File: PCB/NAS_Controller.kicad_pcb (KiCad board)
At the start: 4 copper layers, 119.5 x 99.6 mm, 350 parts, among them J1 Barrel_Jack, J10 Conn_01x10, J11 10103594-0001LF, J13 Conn_01x03, J14 20021121-00020C4LF, J15 Conn_01x03, J18 M20-9990246, J2 Conn_01x04, J3 105133-0011, J4 10103594-0001LF, J5 NPPN101BFCN-RC, J6 NPPN101BFCN-RC, J7 Conn_01x03, J8 PPTC081LFBN-RC, J9 PPTC081LFBN-RC, Q1 DMN6068LK3-13, Q10 AOD409, Q11 DMG1026UV-7, Q12 DMG1026UV-7, Q13 DMN6068LK3-13, Q14 DMG1026UV-7, Q2 DMN6068LK3-13, Q3 MMBT3904-TP, Q8 AOD409, Q9 AOD409, SW1 SW_SP3T_1COM_234, U1 ZXCT1110, U10 TS5A3357DCUR, U11 PCA6416APW,118, U12 ZXGD3009E6TA, U13 TS462CDT, U14 AP65211AWU-7, U15 RT7258GSP, U16 RT7258GSP, U17 LM3481MM, U2 TS462CDT, U3 AZ1084CD-3.3, U4 TS462CDT, U5 TS462CDT, U6 TMS320F28035PAGS, U7 MB85RS16, U8 CY7C65634-48AXCT, U9 TS5A3357DCUR, Y1 12MHz

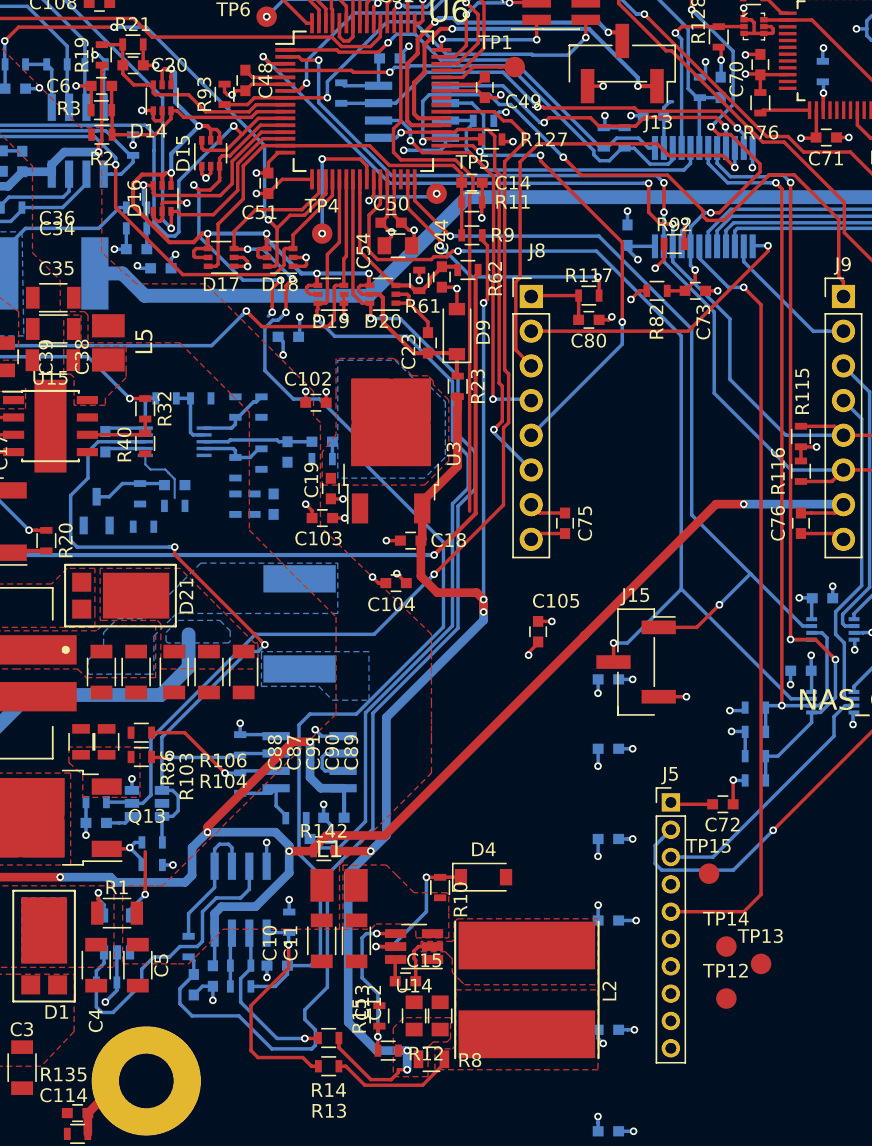
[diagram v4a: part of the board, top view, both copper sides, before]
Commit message: Layout... finished routing, now need to stitch vias, reveiew pours and then silkscreen.
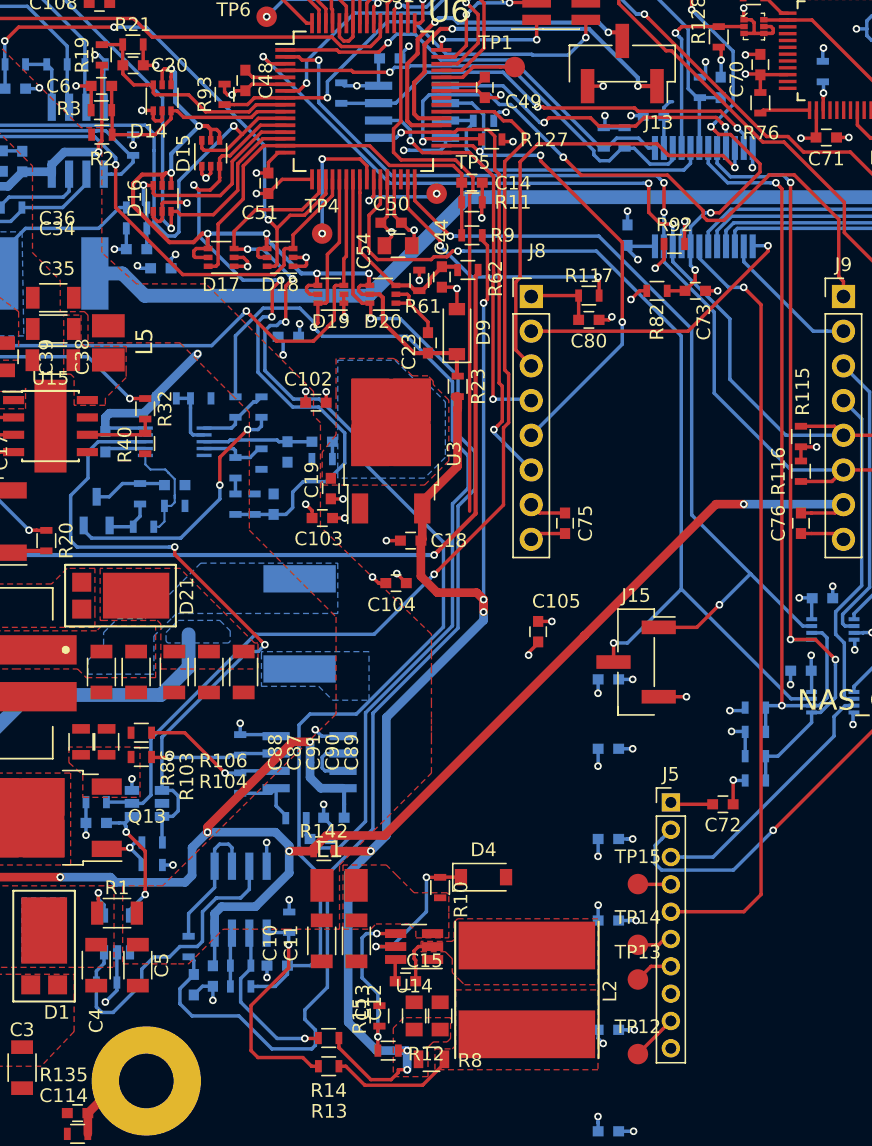
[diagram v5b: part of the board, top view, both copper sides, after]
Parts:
- moved TP13 9.09 mm to (82.4, 86.2)
- moved TP12 7.65 mm to (82.4, 91.7)
- moved TP14 6.48 mm to (82.4, 83.7)
- moved TP15 5.26 mm to (82.4, 79.2)
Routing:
- net ADC_SEPIC_V: track 24.0 -> 49.1 mm
- net Net-(Q3-Pad2): track 0.00 -> 19.4 mm, vias 0 -> 2
- net ADC_SEPIC_I: track 65.6 -> 78.2 mm
- net Vin: track 28.9 -> 38.7 mm, vias 15 -> 17
- net Net-(Q3-Pad1): track 0.00 -> 3.64 mm
- net Net-(R112-Pad1): track 4.86 -> 8.30 mm
- net Net-(J5-Pad9): track 0.00 -> 3.42 mm
- net Net-(J5-Pad7): track 0.00 -> 2.81 mm
- net Net-(J5-Pad6): track 0.00 -> 2.59 mm
- net Net-(J5-Pad4): track 0.00 -> 2.42 mm
- net V_SEPIC: track 36.1 -> 37.3 mm
- net ADC_BATT_I: track 55.5 -> 56.4 mm
- net +3V3: track 108.8 -> 108.4 mm, vias 43 -> 44

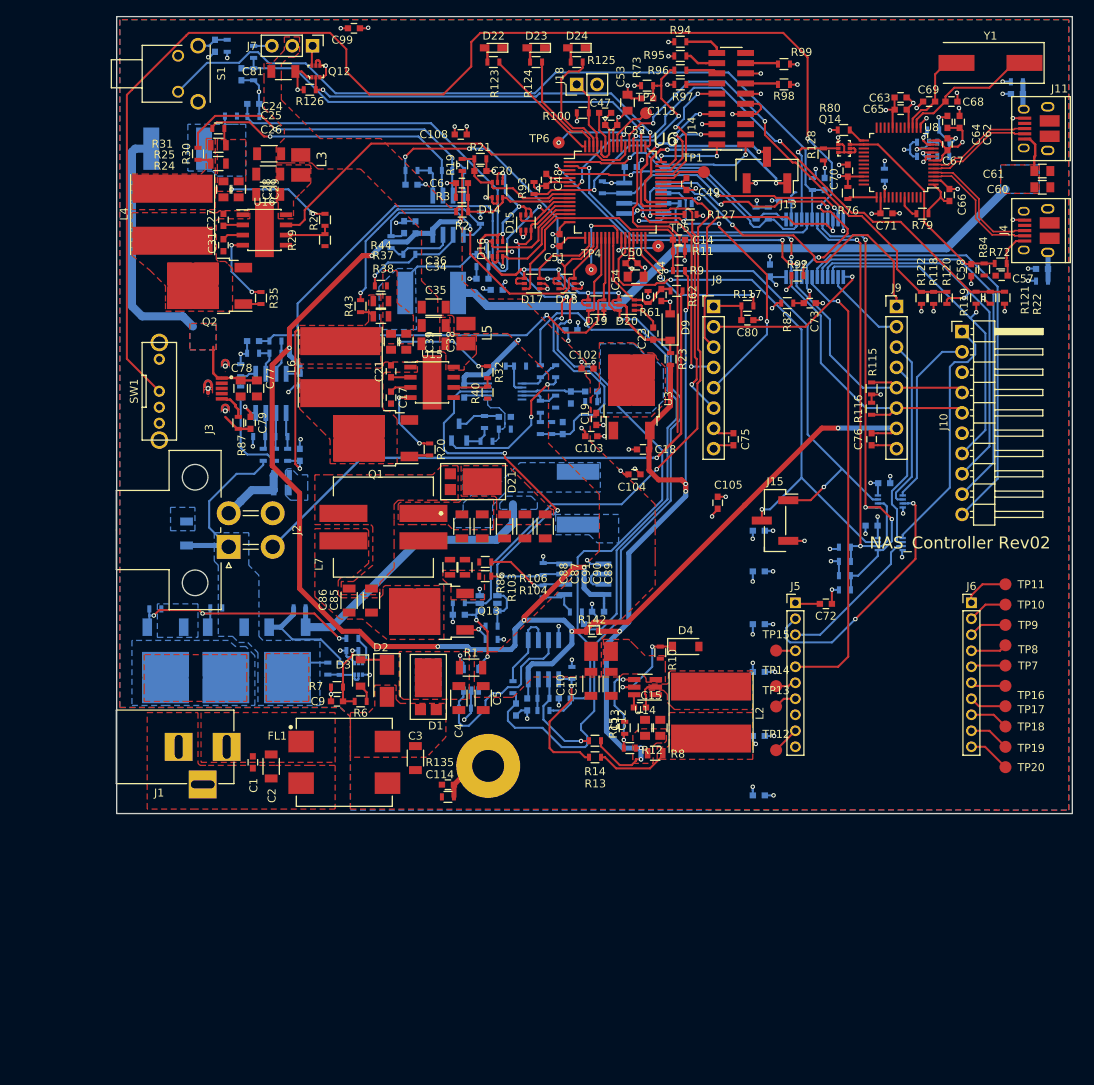
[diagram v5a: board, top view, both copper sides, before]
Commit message: Added stitching vias; one unconnected net left, then silkscreen.
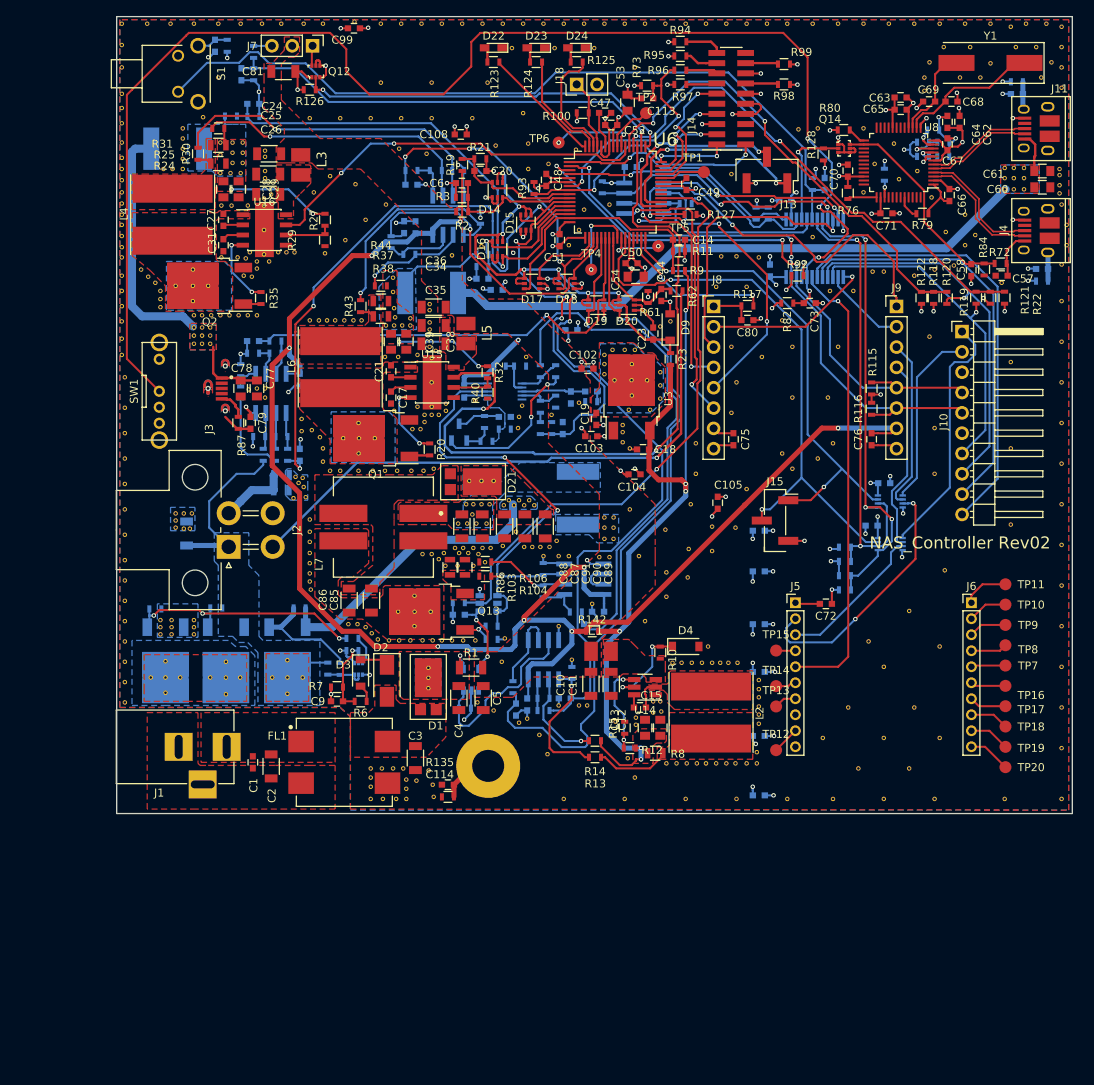
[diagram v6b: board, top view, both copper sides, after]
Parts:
- added REF**: VIA_12_22, CustomFootprints:VIA_12_22, F.Cu at (113.4, 20.2)
- added REF**: VIA_12_22, CustomFootprints:VIA_12_22, F.Cu at (9.65, 75.4)
- added REF**: VIA_12_22, CustomFootprints:VIA_12_22, F.Cu at (111.8, 43.2)
- added REF**: VIA_12_22, CustomFootprints:VIA_12_22, F.Cu at (111.8, 54.0)
- added REF**: VIA_12_22, CustomFootprints:VIA_12_22, F.Cu at (111.8, 63.5)
- added REF**: VIA_12_22, CustomFootprints:VIA_12_22, F.Cu at (103.5, 69.2)
- added REF**: VIA_12_22, CustomFootprints:VIA_12_22, F.Cu at (99.1, 74.3)
- added REF**: VIA_12_22, CustomFootprints:VIA_12_22, F.Cu at (94.0, 78.1)
- added REF**: VIA_12_22, CustomFootprints:VIA_12_22, F.Cu at (102.9, 78.7)
- added REF**: VIA_12_22, CustomFootprints:VIA_12_22, F.Cu at (95.9, 81.3)
- added REF**: VIA_12_22, CustomFootprints:VIA_12_22, F.Cu at (91.4, 86.4)
- added REF**: VIA_12_22, CustomFootprints:VIA_12_22, F.Cu at (99.7, 86.4)
- added REF**: VIA_12_22, CustomFootprints:VIA_12_22, F.Cu at (9.65, 76.3)
- added REF**: VIA_12_22, CustomFootprints:VIA_12_22, F.Cu at (102.9, 90.2)
- added REF**: VIA_12_22, CustomFootprints:VIA_12_22, F.Cu at (95.9, 90.2)
- added REF**: VIA_12_22, CustomFootprints:VIA_12_22, F.Cu at (88.3, 90.2)
- added REF**: VIA_12_22, CustomFootprints:VIA_12_22, F.Cu at (99.1, 94.0)
- added REF**: VIA_12_22, CustomFootprints:VIA_12_22, F.Cu at (92.7, 94.0)
- added REF**: VIA_12_22, CustomFootprints:VIA_12_22, F.Cu at (118.7, 28.6)
- added REF**: VIA_12_22, CustomFootprints:VIA_12_22, F.Cu at (118.7, 26.0)
- added REF**: VIA_12_22, CustomFootprints:VIA_12_22, F.Cu at (118.1, 23.5)
- added REF**: VIA_12_22, CustomFootprints:VIA_12_22, F.Cu at (118.1, 6.35)
- added REF**: VIA_12_22, CustomFootprints:VIA_12_22, F.Cu at (118.1, 3.81)
- added REF**: VIA_12_22, CustomFootprints:VIA_12_22, F.Cu at (9.65, 77.2)
- added REF**: VIA_12_22, CustomFootprints:VIA_12_22, F.Cu at (116.2, 0.89)
- added REF**: VIA_12_22, CustomFootprints:VIA_12_22, F.Cu at (113.7, 0.89)
- added REF**: VIA_12_22, CustomFootprints:VIA_12_22, F.Cu at (109.2, 0.89)
- added REF**: VIA_12_22, CustomFootprints:VIA_12_22, F.Cu at (106.0, 0.89)
- added REF**: VIA_12_22, CustomFootprints:VIA_12_22, F.Cu at (102.9, 0.89)
- added REF**: VIA_12_22, CustomFootprints:VIA_12_22, F.Cu at (99.7, 0.89)
- added REF**: VIA_12_22, CustomFootprints:VIA_12_22, F.Cu at (96.5, 0.89)
- added REF**: VIA_12_22, CustomFootprints:VIA_12_22, F.Cu at (93.3, 0.89)
- added REF**: VIA_12_22, CustomFootprints:VIA_12_22, F.Cu at (90.2, 0.89)
- added REF**: VIA_12_22, CustomFootprints:VIA_12_22, F.Cu at (87.0, 0.89)
- added REF**: VIA_12_22, CustomFootprints:VIA_12_22, F.Cu at (5.46, 76.3)
- added REF**: VIA_12_22, CustomFootprints:VIA_12_22, F.Cu at (83.8, 0.89)
- added REF**: VIA_12_22, CustomFootprints:VIA_12_22, F.Cu at (81.3, 0.89)
- added REF**: VIA_12_22, CustomFootprints:VIA_12_22, F.Cu at (78.7, 0.89)
- added REF**: VIA_12_22, CustomFootprints:VIA_12_22, F.Cu at (76.2, 0.89)
- added REF**: VIA_12_22, CustomFootprints:VIA_12_22, F.Cu at (73.7, 0.89)
- added REF**: VIA_12_22, CustomFootprints:VIA_12_22, F.Cu at (71.1, 0.89)
- added REF**: VIA_12_22, CustomFootprints:VIA_12_22, F.Cu at (68.6, 0.89)
- added REF**: VIA_12_22, CustomFootprints:VIA_12_22, F.Cu at (66.0, 0.89)
- added REF**: VIA_12_22, CustomFootprints:VIA_12_22, F.Cu at (63.5, 0.89)
- added REF**: VIA_12_22, CustomFootprints:VIA_12_22, F.Cu at (61.0, 0.89)
- added REF**: VIA_12_22, CustomFootprints:VIA_12_22, F.Cu at (5.46, 75.4)
- added REF**: VIA_12_22, CustomFootprints:VIA_12_22, F.Cu at (58.4, 0.89)
- added REF**: VIA_12_22, CustomFootprints:VIA_12_22, F.Cu at (55.9, 0.89)
- added REF**: VIA_12_22, CustomFootprints:VIA_12_22, F.Cu at (53.3, 0.89)
- added REF**: VIA_12_22, CustomFootprints:VIA_12_22, F.Cu at (50.8, 0.89)
- added REF**: VIA_12_22, CustomFootprints:VIA_12_22, F.Cu at (48.3, 0.89)
- added REF**: VIA_12_22, CustomFootprints:VIA_12_22, F.Cu at (45.7, 0.89)
- added REF**: VIA_12_22, CustomFootprints:VIA_12_22, F.Cu at (43.2, 0.89)
- added REF**: VIA_12_22, CustomFootprints:VIA_12_22, F.Cu at (40.6, 0.89)
- added REF**: VIA_12_22, CustomFootprints:VIA_12_22, F.Cu at (38.1, 0.89)
- added REF**: VIA_12_22, CustomFootprints:VIA_12_22, F.Cu at (35.6, 0.89)
- added REF**: VIA_12_22, CustomFootprints:VIA_12_22, F.Cu at (6.86, 75.4)
- added REF**: VIA_12_22, CustomFootprints:VIA_12_22, F.Cu at (33.0, 0.89)
- added REF**: VIA_12_22, CustomFootprints:VIA_12_22, F.Cu at (29.7, 0.64)
- added REF**: VIA_12_22, CustomFootprints:VIA_12_22, F.Cu at (25.8, 0.89)
- added REF**: VIA_12_22, CustomFootprints:VIA_12_22, F.Cu at (23.4, 0.89)
- added REF**: VIA_12_22, CustomFootprints:VIA_12_22, F.Cu at (20.6, 0.89)
- added REF**: VIA_12_22, CustomFootprints:VIA_12_22, F.Cu at (18.2, 0.89)
- added REF**: VIA_12_22, CustomFootprints:VIA_12_22, F.Cu at (15.5, 0.89)
- added REF**: VIA_12_22, CustomFootprints:VIA_12_22, F.Cu at (12.7, 0.89)
- added REF**: VIA_12_22, CustomFootprints:VIA_12_22, F.Cu at (9.65, 0.89)
- added REF**: VIA_12_22, CustomFootprints:VIA_12_22, F.Cu at (6.73, 0.89)
- added REF**: VIA_12_22, CustomFootprints:VIA_12_22, F.Cu at (6.86, 76.3)
- added REF**: VIA_12_22, CustomFootprints:VIA_12_22, F.Cu at (3.81, 0.89)
- added REF**: VIA_12_22, CustomFootprints:VIA_12_22, F.Cu at (0.64, 0.89)
- added REF**: VIA_12_22, CustomFootprints:VIA_12_22, F.Cu at (0.64, 3.56)
- added REF**: VIA_12_22, CustomFootprints:VIA_12_22, F.Cu at (0.64, 6.35)
- added REF**: VIA_12_22, CustomFootprints:VIA_12_22, F.Cu at (0.64, 9.65)
- added REF**: VIA_12_22, CustomFootprints:VIA_12_22, F.Cu at (0.64, 11.4)
- added REF**: VIA_12_22, CustomFootprints:VIA_12_22, F.Cu at (0.64, 13.3)
- added REF**: VIA_12_22, CustomFootprints:VIA_12_22, F.Cu at (0.64, 32.4)
- added REF**: VIA_12_22, CustomFootprints:VIA_12_22, F.Cu at (0.64, 34.3)
- added REF**: VIA_12_22, CustomFootprints:VIA_12_22, F.Cu at (0.64, 36.2)
- added REF**: VIA_12_22, CustomFootprints:VIA_12_22, F.Cu at (6.86, 77.2)
- added REF**: VIA_12_22, CustomFootprints:VIA_12_22, F.Cu at (0.64, 38.1)
- added REF**: VIA_12_22, CustomFootprints:VIA_12_22, F.Cu at (0.64, 40.3)
- added REF**: VIA_12_22, CustomFootprints:VIA_12_22, F.Cu at (0.64, 42.3)
- added REF**: VIA_12_22, CustomFootprints:VIA_12_22, F.Cu at (1.02, 45.1)
- added REF**: VIA_12_22, CustomFootprints:VIA_12_22, F.Cu at (1.02, 48.9)
- added REF**: VIA_12_22, CustomFootprints:VIA_12_22, F.Cu at (1.02, 52.1)
- added REF**: VIA_12_22, CustomFootprints:VIA_12_22, F.Cu at (1.02, 55.2)
- added REF**: VIA_12_22, CustomFootprints:VIA_12_22, F.Cu at (1.02, 58.4)
- added REF**: VIA_12_22, CustomFootprints:VIA_12_22, F.Cu at (1.02, 61.6)
- added REF**: VIA_12_22, CustomFootprints:VIA_12_22, F.Cu at (1.02, 64.8)
- added REF**: VIA_12_22, CustomFootprints:VIA_12_22, F.Cu at (5.46, 77.2)
- added REF**: VIA_12_22, CustomFootprints:VIA_12_22, F.Cu at (1.02, 67.9)
- added REF**: VIA_12_22, CustomFootprints:VIA_12_22, F.Cu at (1.02, 70.5)
- added REF**: VIA_12_22, CustomFootprints:VIA_12_22, F.Cu at (1.02, 73.0)
- added REF**: VIA_12_22, CustomFootprints:VIA_12_22, F.Cu at (1.02, 75.6)
- added REF**: VIA_12_22, CustomFootprints:VIA_12_22, F.Cu at (1.02, 78.1)
- added REF**: VIA_12_22, CustomFootprints:VIA_12_22, F.Cu at (1.02, 80.6)
- added REF**: VIA_12_22, CustomFootprints:VIA_12_22, F.Cu at (1.02, 83.2)
- added REF**: VIA_12_22, CustomFootprints:VIA_12_22, F.Cu at (1.02, 85.7)
- added REF**: VIA_12_22, CustomFootprints:VIA_12_22, F.Cu at (6.10, 84.5)
- added REF**: VIA_12_22, CustomFootprints:VIA_12_22, F.Cu at (6.10, 80.6)
- added REF**: VIA_12_22, CustomFootprints:VIA_12_22, F.Cu at (45.6, 28.7)
- added REF**: VIA_12_22, CustomFootprints:VIA_12_22, F.Cu at (4.25, 82.6)
- added REF**: VIA_12_22, CustomFootprints:VIA_12_22, F.Cu at (7.94, 82.6)
- added REF**: VIA_12_22, CustomFootprints:VIA_12_22, F.Cu at (6.10, 82.6)
- added REF**: VIA_12_22, CustomFootprints:VIA_12_22, F.Cu at (13.7, 84.7)
- added REF**: VIA_12_22, CustomFootprints:VIA_12_22, F.Cu at (13.7, 80.6)
- added REF**: VIA_12_22, CustomFootprints:VIA_12_22, F.Cu at (11.7, 82.6)
- added REF**: VIA_12_22, CustomFootprints:VIA_12_22, F.Cu at (15.4, 82.6)
- added REF**: VIA_12_22, CustomFootprints:VIA_12_22, F.Cu at (13.7, 82.6)
- added REF**: VIA_12_22, CustomFootprints:VIA_12_22, F.Cu at (21.3, 84.6)
- added REF**: VIA_12_22, CustomFootprints:VIA_12_22, F.Cu at (21.3, 80.5)
- added REF**: VIA_12_22, CustomFootprints:VIA_12_22, F.Cu at (113.4, 18.9)
- added REF**: VIA_12_22, CustomFootprints:VIA_12_22, F.Cu at (62.1, 63.9)
- added REF**: VIA_12_22, CustomFootprints:VIA_12_22, F.Cu at (19.4, 82.6)
- added REF**: VIA_12_22, CustomFootprints:VIA_12_22, F.Cu at (23.2, 82.6)
- added REF**: VIA_12_22, CustomFootprints:VIA_12_22, F.Cu at (21.3, 82.6)
- added REF**: VIA_12_22, CustomFootprints:VIA_12_22, F.Cu at (41.1, 68.6)
- added REF**: VIA_12_22, CustomFootprints:VIA_12_22, F.Cu at (46.0, 68.2)
- added REF**: VIA_12_22, CustomFootprints:VIA_12_22, F.Cu at (44.6, 68.6)
- added REF**: VIA_12_22, CustomFootprints:VIA_12_22, F.Cu at (42.6, 68.6)
- added REF**: VIA_12_22, CustomFootprints:VIA_12_22, F.Cu at (39.0, 83.9)
- added REF**: VIA_12_22, CustomFootprints:VIA_12_22, F.Cu at (39.0, 81.4)
- added REF**: VIA_12_22, CustomFootprints:VIA_12_22, F.Cu at (39.0, 82.6)
- added REF**: VIA_12_22, CustomFootprints:VIA_12_22, F.Cu at (62.1, 65.3)
- added REF**: VIA_12_22, CustomFootprints:VIA_12_22, F.Cu at (37.2, 76.2)
- added REF**: VIA_12_22, CustomFootprints:VIA_12_22, F.Cu at (37.2, 72.4)
- added REF**: VIA_12_22, CustomFootprints:VIA_12_22, F.Cu at (35.2, 74.4)
- added REF**: VIA_12_22, CustomFootprints:VIA_12_22, F.Cu at (39.2, 74.4)
- added REF**: VIA_12_22, CustomFootprints:VIA_12_22, F.Cu at (34.5, 32.6)
- added REF**: VIA_12_22, CustomFootprints:VIA_12_22, F.Cu at (34.5, 34.4)
- added REF**: VIA_12_22, CustomFootprints:VIA_12_22, F.Cu at (34.7, 36.4)
- added REF**: VIA_12_22, CustomFootprints:VIA_12_22, F.Cu at (34.8, 37.6)
- added REF**: VIA_12_22, CustomFootprints:VIA_12_22, F.Cu at (36.7, 37.7)
- added REF**: VIA_12_22, CustomFootprints:VIA_12_22, F.Cu at (36.7, 38.6)
- added REF**: VIA_12_22, CustomFootprints:VIA_12_22, F.Cu at (61.0, 65.3)
- added REF**: VIA_12_22, CustomFootprints:VIA_12_22, F.Cu at (35.7, 38.6)
- added REF**: VIA_12_22, CustomFootprints:VIA_12_22, F.Cu at (34.7, 38.6)
- added REF**: VIA_12_22, CustomFootprints:VIA_12_22, F.Cu at (33.7, 38.6)
- added REF**: VIA_12_22, CustomFootprints:VIA_12_22, F.Cu at (52.2, 61.1)
- added REF**: VIA_12_22, CustomFootprints:VIA_12_22, F.Cu at (51.6, 60.5)
- added REF**: VIA_12_22, CustomFootprints:VIA_12_22, F.Cu at (50.9, 61.1)
- added REF**: VIA_12_22, CustomFootprints:VIA_12_22, F.Cu at (50.3, 60.5)
- added REF**: VIA_12_22, CustomFootprints:VIA_12_22, F.Cu at (49.7, 61.1)
- added REF**: VIA_12_22, CustomFootprints:VIA_12_22, F.Cu at (49.0, 60.5)
- added REF**: VIA_12_22, CustomFootprints:VIA_12_22, F.Cu at (48.4, 61.1)
- added REF**: VIA_12_22, CustomFootprints:VIA_12_22, F.Cu at (61.0, 63.9)
- added REF**: VIA_12_22, CustomFootprints:VIA_12_22, F.Cu at (44.1, 58.0)
- added REF**: VIA_12_22, CustomFootprints:VIA_12_22, F.Cu at (47.1, 58.0)
- added REF**: VIA_12_22, CustomFootprints:VIA_12_22, F.Cu at (45.6, 58.0)
- added REF**: VIA_12_22, CustomFootprints:VIA_12_22, F.Cu at (44.5, 62.2)
- added REF**: VIA_12_22, CustomFootprints:VIA_12_22, F.Cu at (43.7, 61.0)
- added REF**: VIA_12_22, CustomFootprints:VIA_12_22, F.Cu at (44.6, 61.0)
- added REF**: VIA_12_22, CustomFootprints:VIA_12_22, F.Cu at (45.6, 61.0)
- added REF**: VIA_12_22, CustomFootprints:VIA_12_22, F.Cu at (46.6, 61.0)
- added REF**: VIA_12_22, CustomFootprints:VIA_12_22, F.Cu at (46.2, 63.4)
- added REF**: VIA_12_22, CustomFootprints:VIA_12_22, F.Cu at (45.0, 63.4)
- added REF**: VIA_12_22, CustomFootprints:VIA_12_22, F.Cu at (62.1, 62.6)
- added REF**: VIA_12_22, CustomFootprints:VIA_12_22, F.Cu at (43.8, 63.4)
- added REF**: VIA_12_22, CustomFootprints:VIA_12_22, F.Cu at (42.7, 63.4)
- added REF**: VIA_12_22, CustomFootprints:VIA_12_22, F.Cu at (64.4, 47.4)
- added REF**: VIA_12_22, CustomFootprints:VIA_12_22, F.Cu at (64.4, 43.4)
- added REF**: VIA_12_22, CustomFootprints:VIA_12_22, F.Cu at (66.3, 45.5)
- added REF**: VIA_12_22, CustomFootprints:VIA_12_22, F.Cu at (62.2, 45.5)
- added REF**: VIA_12_22, CustomFootprints:VIA_12_22, F.Cu at (64.4, 45.4)
- added REF**: VIA_12_22, CustomFootprints:VIA_12_22, F.Cu at (61.0, 43.4)
- added REF**: VIA_12_22, CustomFootprints:VIA_12_22, F.Cu at (61.0, 44.7)
- added REF**: VIA_12_22, CustomFootprints:VIA_12_22, F.Cu at (61.0, 42.3)
- added REF**: VIA_12_22, CustomFootprints:VIA_12_22, F.Cu at (61.0, 62.6)
- added REF**: VIA_12_22, CustomFootprints:VIA_12_22, F.Cu at (62.0, 41.7)
- added REF**: VIA_12_22, CustomFootprints:VIA_12_22, F.Cu at (63.5, 41.7)
- added REF**: VIA_12_22, CustomFootprints:VIA_12_22, F.Cu at (64.8, 41.7)
- added REF**: VIA_12_22, CustomFootprints:VIA_12_22, F.Cu at (67.9, 44.5)
- added REF**: VIA_12_22, CustomFootprints:VIA_12_22, F.Cu at (67.9, 46.1)
- added REF**: VIA_12_22, CustomFootprints:VIA_12_22, F.Cu at (67.9, 47.8)
- added REF**: VIA_12_22, CustomFootprints:VIA_12_22, F.Cu at (64.0, 49.1)
- added REF**: VIA_12_22, CustomFootprints:VIA_12_22, F.Cu at (66.7, 49.1)
- added REF**: VIA_12_22, CustomFootprints:VIA_12_22, F.Cu at (64.1, 61.6)
- added REF**: VIA_12_22, CustomFootprints:VIA_12_22, F.Cu at (65.3, 67.4)
- added REF**: VIA_12_22, CustomFootprints:VIA_12_22, F.Cu at (41.9, 29.8)
- added REF**: VIA_12_22, CustomFootprints:VIA_12_22, F.Cu at (74.4, 63.8)
- added REF**: VIA_12_22, CustomFootprints:VIA_12_22, F.Cu at (71.5, 66.5)
- added REF**: VIA_12_22, CustomFootprints:VIA_12_22, F.Cu at (68.7, 69.5)
- added REF**: VIA_12_22, CustomFootprints:VIA_12_22, F.Cu at (77.3, 63.9)
- added REF**: VIA_12_22, CustomFootprints:VIA_12_22, F.Cu at (74.4, 66.8)
- added REF**: VIA_12_22, CustomFootprints:VIA_12_22, F.Cu at (71.4, 70.1)
- added REF**: VIA_12_22, CustomFootprints:VIA_12_22, F.Cu at (68.7, 72.5)
- added REF**: VIA_12_22, CustomFootprints:VIA_12_22, F.Cu at (66.0, 75.6)
- added REF**: VIA_12_22, CustomFootprints:VIA_12_22, F.Cu at (48.1, 80.6)
- added REF**: VIA_12_22, CustomFootprints:VIA_12_22, F.Cu at (52.8, 89.8)
- added REF**: VIA_12_22, CustomFootprints:VIA_12_22, F.Cu at (9.53, 35.6)
- added REF**: VIA_12_22, CustomFootprints:VIA_12_22, F.Cu at (53.8, 92.2)
- added REF**: VIA_12_22, CustomFootprints:VIA_12_22, F.Cu at (55.9, 97.8)
- added REF**: VIA_12_22, CustomFootprints:VIA_12_22, F.Cu at (64.8, 95.1)
- added REF**: VIA_12_22, CustomFootprints:VIA_12_22, F.Cu at (63.5, 97.8)
- added REF**: VIA_12_22, CustomFootprints:VIA_12_22, F.Cu at (71.1, 97.8)
- added REF**: VIA_12_22, CustomFootprints:VIA_12_22, F.Cu at (77.5, 97.8)
- added REF**: VIA_12_22, CustomFootprints:VIA_12_22, F.Cu at (83.8, 97.8)
- added REF**: VIA_12_22, CustomFootprints:VIA_12_22, F.Cu at (89.5, 97.8)
- added REF**: VIA_12_22, CustomFootprints:VIA_12_22, F.Cu at (95.9, 97.8)
- added REF**: VIA_12_22, CustomFootprints:VIA_12_22, F.Cu at (102.2, 97.8)
- added REF**: VIA_12_22, CustomFootprints:VIA_12_22, F.Cu at (9.53, 31.6)
- added REF**: VIA_12_22, CustomFootprints:VIA_12_22, F.Cu at (111.0, 97.8)
- added REF**: VIA_12_22, CustomFootprints:VIA_12_22, F.Cu at (118.1, 97.8)
- added REF**: VIA_12_22, CustomFootprints:VIA_12_22, F.Cu at (118.1, 91.4)
- added REF**: VIA_12_22, CustomFootprints:VIA_12_22, F.Cu at (118.1, 86.4)
- added REF**: VIA_12_22, CustomFootprints:VIA_12_22, F.Cu at (118.1, 81.3)
- added REF**: VIA_12_22, CustomFootprints:VIA_12_22, F.Cu at (118.1, 76.2)
- added REF**: VIA_12_22, CustomFootprints:VIA_12_22, F.Cu at (118.1, 71.1)
- added REF**: VIA_12_22, CustomFootprints:VIA_12_22, F.Cu at (118.1, 66.0)
- added REF**: VIA_12_22, CustomFootprints:VIA_12_22, F.Cu at (118.1, 61.0)
- added REF**: VIA_12_22, CustomFootprints:VIA_12_22, F.Cu at (118.1, 55.9)
- added REF**: VIA_12_22, CustomFootprints:VIA_12_22, F.Cu at (7.37, 33.7)
- added REF**: VIA_12_22, CustomFootprints:VIA_12_22, F.Cu at (118.1, 50.8)
- added REF**: VIA_12_22, CustomFootprints:VIA_12_22, F.Cu at (118.1, 45.7)
- added REF**: VIA_12_22, CustomFootprints:VIA_12_22, F.Cu at (118.1, 40.6)
- added REF**: VIA_12_22, CustomFootprints:VIA_12_22, F.Cu at (118.1, 35.6)
- added REF**: VIA_12_22, CustomFootprints:VIA_12_22, F.Cu at (118.1, 31.0)
- added REF**: VIA_12_22, CustomFootprints:VIA_12_22, F.Cu at (118.1, 8.89)
- added REF**: VIA_12_22, CustomFootprints:VIA_12_22, F.Cu at (116.8, 5.72)
- added REF**: VIA_12_22, CustomFootprints:VIA_12_22, F.Cu at (115.6, 7.62)
- added REF**: VIA_12_22, CustomFootprints:VIA_12_22, F.Cu at (105.4, 7.62)
- added REF**: VIA_12_22, CustomFootprints:VIA_12_22, F.Cu at (108.0, 7.62)
- added REF**: VIA_12_22, CustomFootprints:VIA_12_22, F.Cu at (112.1, 18.9)
- added REF**: VIA_12_22, CustomFootprints:VIA_12_22, F.Cu at (11.4, 33.7)
- added REF**: VIA_12_22, CustomFootprints:VIA_12_22, F.Cu at (109.2, 5.84)
- added REF**: VIA_12_22, CustomFootprints:VIA_12_22, F.Cu at (101.0, 9.27)
- added REF**: VIA_12_22, CustomFootprints:VIA_12_22, F.Cu at (101.0, 7.62)
- added REF**: VIA_12_22, CustomFootprints:VIA_12_22, F.Cu at (101.6, 5.72)
- added REF**: VIA_12_22, CustomFootprints:VIA_12_22, F.Cu at (103.4, 3.81)
- added REF**: VIA_12_22, CustomFootprints:VIA_12_22, F.Cu at (106.7, 3.81)
- added REF**: VIA_12_22, CustomFootprints:VIA_12_22, F.Cu at (112.4, 3.81)
- added REF**: VIA_12_22, CustomFootprints:VIA_12_22, F.Cu at (114.9, 3.81)
- added REF**: VIA_12_22, CustomFootprints:VIA_12_22, F.Cu at (111.8, 1.27)
- added REF**: VIA_12_22, CustomFootprints:VIA_12_22, F.Cu at (118.1, 1.27)
- added REF**: VIA_12_22, CustomFootprints:VIA_12_22, F.Cu at (9.53, 33.7)
- added REF**: VIA_12_22, CustomFootprints:VIA_12_22, F.Cu at (83.2, 38.0)
- added REF**: VIA_12_22, CustomFootprints:VIA_12_22, F.Cu at (78.7, 33.8)
- added REF**: VIA_12_22, CustomFootprints:VIA_12_22, F.Cu at (74.9, 33.8)
- added REF**: VIA_12_22, CustomFootprints:VIA_12_22, F.Cu at (75.6, 30.0)
- added REF**: VIA_12_22, CustomFootprints:VIA_12_22, F.Cu at (77.5, 30.0)
- added REF**: VIA_12_22, CustomFootprints:VIA_12_22, F.Cu at (80.3, 30.1)
- added REF**: VIA_12_22, CustomFootprints:VIA_12_22, F.Cu at (87.0, 27.6)
- added REF**: VIA_12_22, CustomFootprints:VIA_12_22, F.Cu at (92.1, 34.3)
- added REF**: VIA_12_22, CustomFootprints:VIA_12_22, F.Cu at (89.2, 34.3)
- added REF**: VIA_12_22, CustomFootprints:VIA_12_22, F.Cu at (94.5, 31.9)
- added REF**: VIA_12_22, CustomFootprints:VIA_12_22, F.Cu at (30.2, 54.6)
- added REF**: VIA_12_22, CustomFootprints:VIA_12_22, F.Cu at (95.9, 31.9)
- added REF**: VIA_12_22, CustomFootprints:VIA_12_22, F.Cu at (99.7, 32.4)
- added REF**: VIA_12_22, CustomFootprints:VIA_12_22, F.Cu at (102.2, 31.6)
- added REF**: VIA_12_22, CustomFootprints:VIA_12_22, F.Cu at (104.6, 31.1)
- added REF**: VIA_12_22, CustomFootprints:VIA_12_22, F.Cu at (110.6, 33.3)
- added REF**: VIA_12_22, CustomFootprints:VIA_12_22, F.Cu at (106.0, 28.6)
- added REF**: VIA_12_22, CustomFootprints:VIA_12_22, F.Cu at (107.3, 27.3)
- added REF**: VIA_12_22, CustomFootprints:VIA_12_22, F.Cu at (106.0, 24.8)
- added REF**: VIA_12_22, CustomFootprints:VIA_12_22, F.Cu at (103.6, 26.9)
- added REF**: VIA_12_22, CustomFootprints:VIA_12_22, F.Cu at (101.9, 22.6)
- added REF**: VIA_12_22, CustomFootprints:VIA_12_22, F.Cu at (30.2, 50.8)
- added REF**: VIA_12_22, CustomFootprints:VIA_12_22, F.Cu at (93.3, 22.0)
- added REF**: VIA_12_22, CustomFootprints:VIA_12_22, F.Cu at (94.7, 18.4)
- added REF**: VIA_12_22, CustomFootprints:VIA_12_22, F.Cu at (97.8, 20.3)
- added REF**: VIA_12_22, CustomFootprints:VIA_12_22, F.Cu at (100.1, 19.3)
- added REF**: VIA_12_22, CustomFootprints:VIA_12_22, F.Cu at (97.2, 15.9)
- added REF**: VIA_12_22, CustomFootprints:VIA_12_22, F.Cu at (93.3, 14.0)
- added REF**: VIA_12_22, CustomFootprints:VIA_12_22, F.Cu at (87.6, 14.0)
- added REF**: VIA_12_22, CustomFootprints:VIA_12_22, F.Cu at (85.2, 14.1)
- added REF**: VIA_12_22, CustomFootprints:VIA_12_22, F.Cu at (64.8, 6.35)
- added REF**: VIA_12_22, CustomFootprints:VIA_12_22, F.Cu at (57.4, 16.6)
- added REF**: VIA_12_22, CustomFootprints:VIA_12_22, F.Cu at (28.3, 52.7)
- added REF**: VIA_12_22, CustomFootprints:VIA_12_22, F.Cu at (54.0, 18.4)
- added REF**: VIA_12_22, CustomFootprints:VIA_12_22, F.Cu at (38.7, 17.1)
- added REF**: VIA_12_22, CustomFootprints:VIA_12_22, F.Cu at (47.4, 16.1)
- added REF**: VIA_12_22, CustomFootprints:VIA_12_22, F.Cu at (44.5, 12.7)
- added REF**: VIA_12_22, CustomFootprints:VIA_12_22, F.Cu at (39.4, 12.7)
- added REF**: VIA_12_22, CustomFootprints:VIA_12_22, F.Cu at (35.6, 12.7)
- added REF**: VIA_12_22, CustomFootprints:VIA_12_22, F.Cu at (31.8, 12.7)
- added REF**: VIA_12_22, CustomFootprints:VIA_12_22, F.Cu at (27.9, 12.7)
- added REF**: VIA_12_22, CustomFootprints:VIA_12_22, F.Cu at (24.1, 12.7)
- added REF**: VIA_12_22, CustomFootprints:VIA_12_22, F.Cu at (35.3, 16.5)
- added REF**: VIA_12_22, CustomFootprints:VIA_12_22, F.Cu at (32.3, 52.7)
- added REF**: VIA_12_22, CustomFootprints:VIA_12_22, F.Cu at (26.7, 19.9)
- added REF**: VIA_12_22, CustomFootprints:VIA_12_22, F.Cu at (24.6, 22.0)
- added REF**: VIA_12_22, CustomFootprints:VIA_12_22, F.Cu at (10.8, 12.6)
- added REF**: VIA_12_22, CustomFootprints:VIA_12_22, F.Cu at (8.26, 14.0)
- added REF**: VIA_12_22, CustomFootprints:VIA_12_22, F.Cu at (8.26, 15.2)
- added REF**: VIA_12_22, CustomFootprints:VIA_12_22, F.Cu at (8.26, 16.5)
- added REF**: VIA_12_22, CustomFootprints:VIA_12_22, F.Cu at (8.26, 17.8)
- added REF**: VIA_12_22, CustomFootprints:VIA_12_22, F.Cu at (5.84, 19.1)
- added REF**: VIA_12_22, CustomFootprints:VIA_12_22, F.Cu at (6.99, 19.1)
- added REF**: VIA_12_22, CustomFootprints:VIA_12_22, F.Cu at (8.26, 19.1)
- added REF**: VIA_12_22, CustomFootprints:VIA_12_22, F.Cu at (30.3, 52.7)
- added REF**: VIA_12_22, CustomFootprints:VIA_12_22, F.Cu at (0.64, 15.7)
- added REF**: VIA_12_22, CustomFootprints:VIA_12_22, F.Cu at (0.64, 17.7)
- added REF**: VIA_12_22, CustomFootprints:VIA_12_22, F.Cu at (0.64, 19.1)
- added REF**: VIA_12_22, CustomFootprints:VIA_12_22, F.Cu at (0.64, 20.4)
- added REF**: VIA_12_22, CustomFootprints:VIA_12_22, F.Cu at (0.64, 22.0)
- added REF**: VIA_12_22, CustomFootprints:VIA_12_22, F.Cu at (0.64, 23.4)
- added REF**: VIA_12_22, CustomFootprints:VIA_12_22, F.Cu at (0.64, 24.8)
- added REF**: VIA_12_22, CustomFootprints:VIA_12_22, F.Cu at (0.64, 26.0)
- added REF**: VIA_12_22, CustomFootprints:VIA_12_22, F.Cu at (0.64, 27.4)
- added REF**: VIA_12_22, CustomFootprints:VIA_12_22, F.Cu at (0.64, 28.8)
- added REF**: VIA_12_22, CustomFootprints:VIA_12_22, F.Cu at (18.5, 47.6)
- added REF**: VIA_12_22, CustomFootprints:VIA_12_22, F.Cu at (0.64, 30.1)
- added REF**: VIA_12_22, CustomFootprints:VIA_12_22, F.Cu at (34.0, 78.0)
- added REF**: VIA_12_22, CustomFootprints:VIA_12_22, F.Cu at (35.3, 78.0)
- added REF**: VIA_12_22, CustomFootprints:VIA_12_22, F.Cu at (36.7, 78.0)
- added REF**: VIA_12_22, CustomFootprints:VIA_12_22, F.Cu at (38.2, 78.0)
- added REF**: VIA_12_22, CustomFootprints:VIA_12_22, F.Cu at (39.5, 78.0)
- added REF**: VIA_12_22, CustomFootprints:VIA_12_22, F.Cu at (40.6, 78.0)
- added REF**: VIA_12_22, CustomFootprints:VIA_12_22, F.Cu at (41.9, 78.0)
- added REF**: VIA_12_22, CustomFootprints:VIA_12_22, F.Cu at (43.3, 78.0)
- added REF**: VIA_12_22, CustomFootprints:VIA_12_22, F.Cu at (44.8, 78.0)
- added REF**: VIA_12_22, CustomFootprints:VIA_12_22, F.Cu at (18.5, 46.5)
- added REF**: VIA_12_22, CustomFootprints:VIA_12_22, F.Cu at (32.6, 77.9)
- added REF**: VIA_12_22, CustomFootprints:VIA_12_22, F.Cu at (31.9, 77.1)
- added REF**: VIA_12_22, CustomFootprints:VIA_12_22, F.Cu at (31.1, 76.3)
- added REF**: VIA_12_22, CustomFootprints:VIA_12_22, F.Cu at (30.1, 75.9)
- added REF**: VIA_12_22, CustomFootprints:VIA_12_22, F.Cu at (29.0, 75.9)
- added REF**: VIA_12_22, CustomFootprints:VIA_12_22, F.Cu at (24.3, 71.6)
- added REF**: VIA_12_22, CustomFootprints:VIA_12_22, F.Cu at (24.1, 70.6)
- added REF**: VIA_12_22, CustomFootprints:VIA_12_22, F.Cu at (24.1, 69.6)
- added REF**: VIA_12_22, CustomFootprints:VIA_12_22, F.Cu at (24.1, 68.3)
- added REF**: VIA_12_22, CustomFootprints:VIA_12_22, F.Cu at (24.1, 67.1)
- added REF**: VIA_12_22, CustomFootprints:VIA_12_22, F.Cu at (17.5, 46.5)
- added REF**: VIA_12_22, CustomFootprints:VIA_12_22, F.Cu at (24.1, 65.7)
- added REF**: VIA_12_22, CustomFootprints:VIA_12_22, F.Cu at (24.1, 64.4)
- added REF**: VIA_12_22, CustomFootprints:VIA_12_22, F.Cu at (24.1, 62.9)
- added REF**: VIA_12_22, CustomFootprints:VIA_12_22, F.Cu at (23.1, 50.3)
- added REF**: VIA_12_22, CustomFootprints:VIA_12_22, F.Cu at (24.4, 51.7)
- added REF**: VIA_12_22, CustomFootprints:VIA_12_22, F.Cu at (23.1, 51.8)
- added REF**: VIA_12_22, CustomFootprints:VIA_12_22, F.Cu at (25.4, 52.6)
- added REF**: VIA_12_22, CustomFootprints:VIA_12_22, F.Cu at (25.8, 54.0)
- added REF**: VIA_12_22, CustomFootprints:VIA_12_22, F.Cu at (25.8, 55.6)
- added REF**: VIA_12_22, CustomFootprints:VIA_12_22, F.Cu at (26.7, 56.8)
- added REF**: VIA_12_22, CustomFootprints:VIA_12_22, F.Cu at (112.1, 20.2)
- added REF**: VIA_12_22, CustomFootprints:VIA_12_22, F.Cu at (16.5, 46.6)
- added REF**: VIA_12_22, CustomFootprints:VIA_12_22, F.Cu at (27.9, 56.8)
- added REF**: VIA_12_22, CustomFootprints:VIA_12_22, F.Cu at (30.2, 56.8)
- added REF**: VIA_12_22, CustomFootprints:VIA_12_22, F.Cu at (32.0, 56.8)
- added REF**: VIA_12_22, CustomFootprints:VIA_12_22, F.Cu at (33.5, 56.8)
- added REF**: VIA_12_22, CustomFootprints:VIA_12_22, F.Cu at (35.1, 56.8)
- added REF**: VIA_12_22, CustomFootprints:VIA_12_22, F.Cu at (36.8, 56.8)
- added REF**: VIA_12_22, CustomFootprints:VIA_12_22, F.Cu at (38.4, 56.8)
- added REF**: VIA_12_22, CustomFootprints:VIA_12_22, F.Cu at (39.6, 56.5)
- added REF**: VIA_12_22, CustomFootprints:VIA_12_22, F.Cu at (24.1, 38.0)
- added REF**: VIA_12_22, CustomFootprints:VIA_12_22, F.Cu at (25.3, 38.0)
- added REF**: VIA_12_22, CustomFootprints:VIA_12_22, F.Cu at (9.65, 39.9)
- added REF**: VIA_12_22, CustomFootprints:VIA_12_22, F.Cu at (26.3, 38.0)
- added REF**: VIA_12_22, CustomFootprints:VIA_12_22, F.Cu at (27.3, 38.0)
- added REF**: VIA_12_22, CustomFootprints:VIA_12_22, F.Cu at (28.4, 38.0)
- added REF**: VIA_12_22, CustomFootprints:VIA_12_22, F.Cu at (29.6, 38.0)
- added REF**: VIA_12_22, CustomFootprints:VIA_12_22, F.Cu at (30.6, 38.0)
- added REF**: VIA_12_22, CustomFootprints:VIA_12_22, F.Cu at (17.5, 37.3)
- added REF**: VIA_12_22, CustomFootprints:VIA_12_22, F.Cu at (16.4, 37.3)
- added REF**: VIA_12_22, CustomFootprints:VIA_12_22, F.Cu at (15.2, 37.3)
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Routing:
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- added copper zone on B.Cu, net Net-(C21-Pad2)
- added copper zone on B.Cu, net Net-(C27-Pad2)

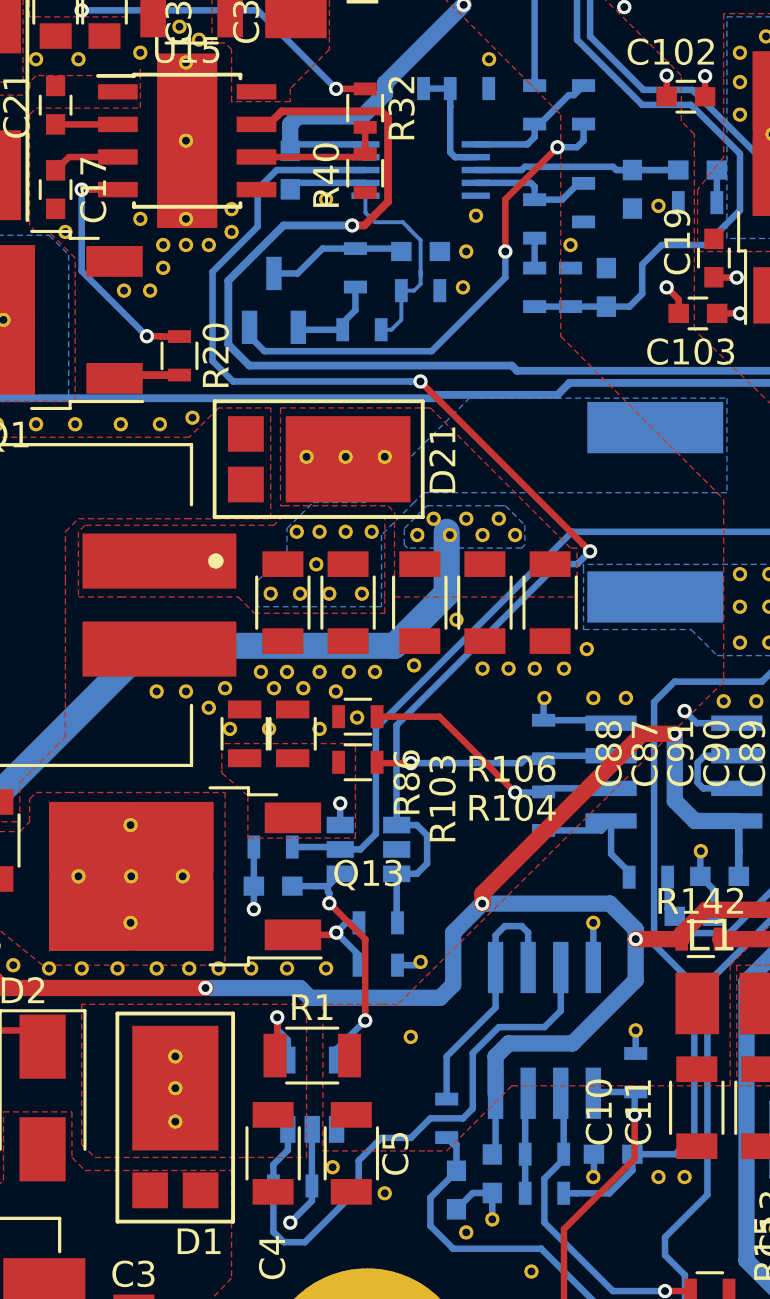
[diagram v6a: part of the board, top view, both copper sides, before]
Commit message: Fixed last missing connection.
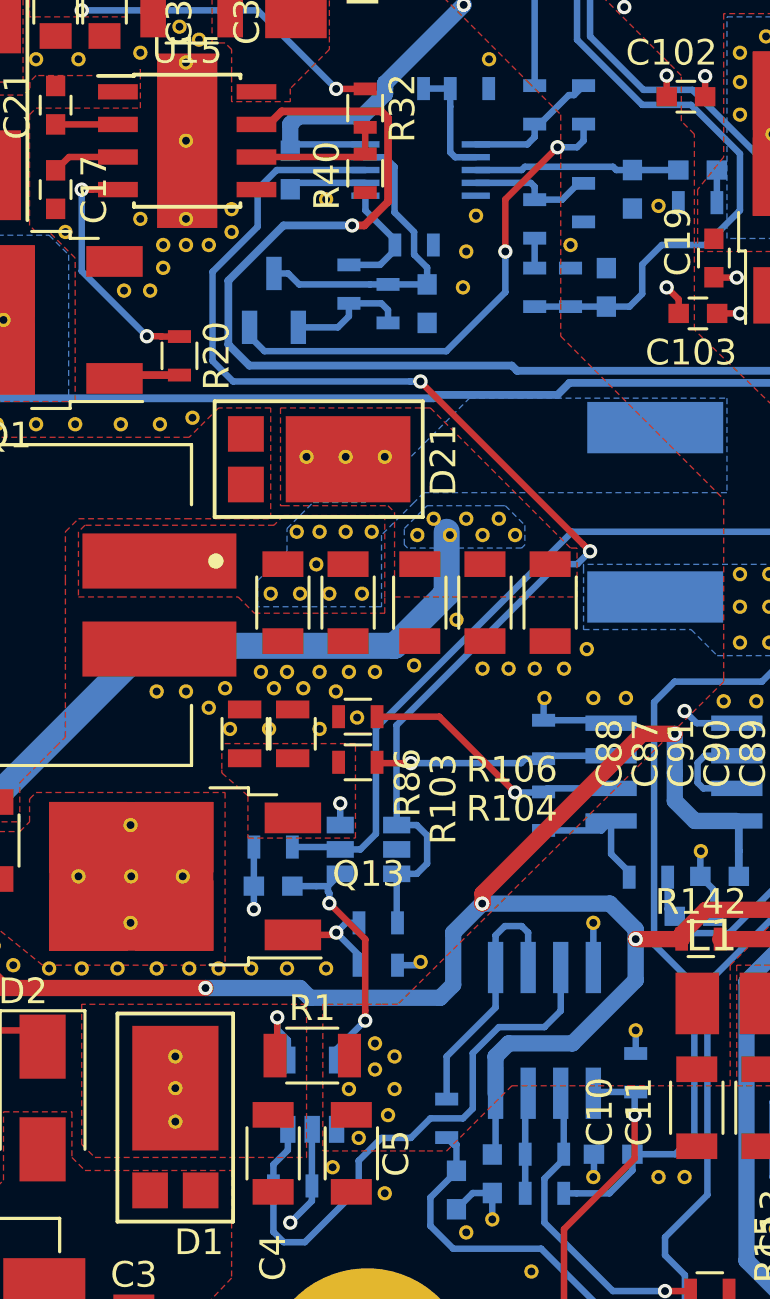
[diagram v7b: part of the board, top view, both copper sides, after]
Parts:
- removed the REF** at (48.1, 80.6)
- added REF**: VIA_12_22, CustomFootprints:VIA_12_22, F.Cu at (46.1, 84.6)
- added REF**: VIA_12_22, CustomFootprints:VIA_12_22, F.Cu at (47.2, 83.7)
- added REF**: VIA_12_22, CustomFootprints:VIA_12_22, F.Cu at (45.7, 82.7)
- added REF**: VIA_12_22, CustomFootprints:VIA_12_22, F.Cu at (47.5, 82.7)
- added REF**: VIA_12_22, CustomFootprints:VIA_12_22, F.Cu at (46.7, 81.9)
- added REF**: VIA_12_22, CustomFootprints:VIA_12_22, F.Cu at (47.5, 81.4)
- added REF**: VIA_12_22, CustomFootprints:VIA_12_22, F.Cu at (46.7, 80.9)
- moved C37 2.05 mm to (48.8, 52.1), turned to 270 degrees
- moved R47 1.89 mm to (47.2, 52.1)
- moved R112 1.85 mm to (45.7, 51.3), turned to 270 degrees
- moved R45 1.80 mm to (48.3, 49.8)
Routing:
- net Net-(C37-Pad1): track 5.41 -> 12.5 mm
- net Net-(R112-Pad1): track 8.30 -> 4.62 mm
- net Net-(Q3-Pad1): track 3.64 -> 4.92 mm
